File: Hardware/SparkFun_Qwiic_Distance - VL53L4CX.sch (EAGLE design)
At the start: 25 parts, among them J2 QWIIC_RIGHT_ANGLE, J4 QWIIC_RIGHT_ANGLE, U1 VL53L4X

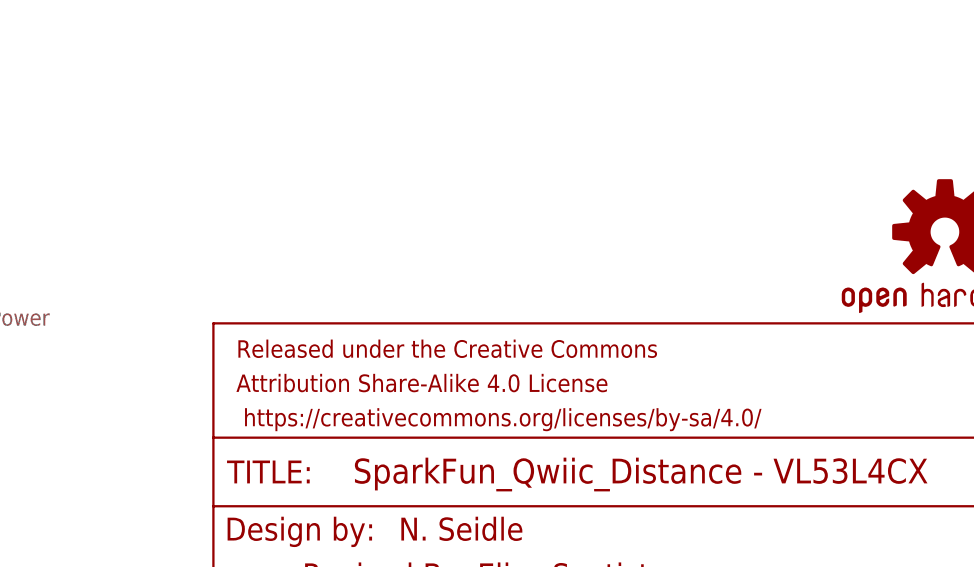
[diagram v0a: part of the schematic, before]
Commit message: Adds silk to the product
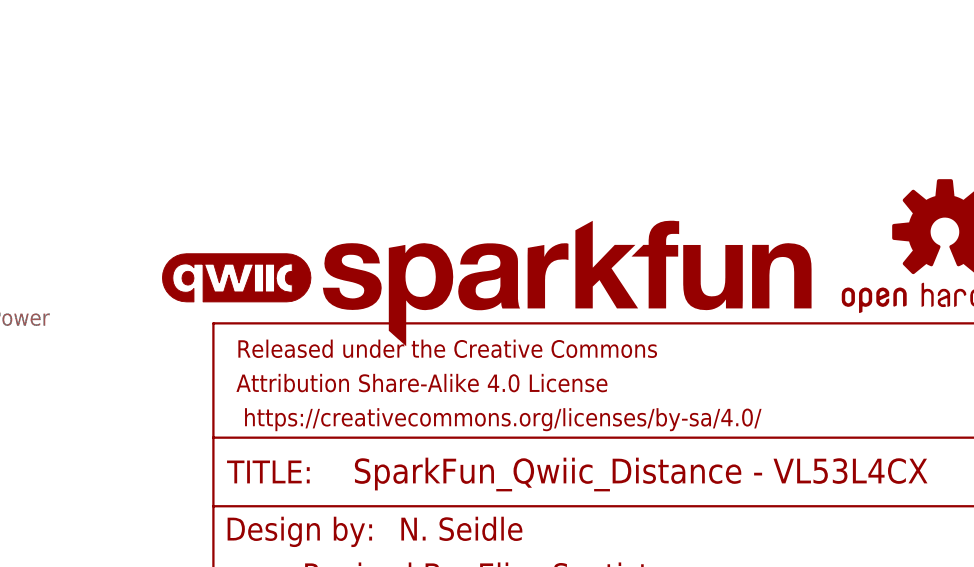
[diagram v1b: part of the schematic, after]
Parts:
- added LOGO2: SFE_LOGO_NAME.1_INCH, SparkFun-Aesthetics:SFE_LOGO_NAME.1_INCH
- added LOGO3: QWIIC_LOGO_4MM, SparkFun-Aesthetics:QWIIC_LOGO_4MM
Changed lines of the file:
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@@
 <part name="JP8" library="SparkFun" deviceset="STAND-OFF" device=""/>
 <part name="JP10" library="SparkFun-Jumpers" deviceset="JUMPER-SMT_2_NC_TRACE" device="_SILK" package3d_urn="urn:adsk.eagle:package:39281/1" value="INT"/>
+<part name="LOGO2" library="SparkFun-Aesthetics" deviceset="SFE_LOGO_NAME" device=".1_INCH"/>
+<part name="LOGO3" library="SparkFun-Aesthetics" deviceset="QWIIC_LOGO" device="_4MM"/>
 </parts>
 <sheets>
@@
 <attribute name="VALUE" x="122.682" y="29.464" size="1.778" layer="96" font="vector" rot="R180"/>
 </instance>
+<instance part="LOGO2" gate="G$1" x="157.48" y="33.02" smashed="yes"/>
+<instance part="LOGO3" gate="G$1" x="149.86" y="40.64" smashed="yes"/>
 </instances>
 <busses>

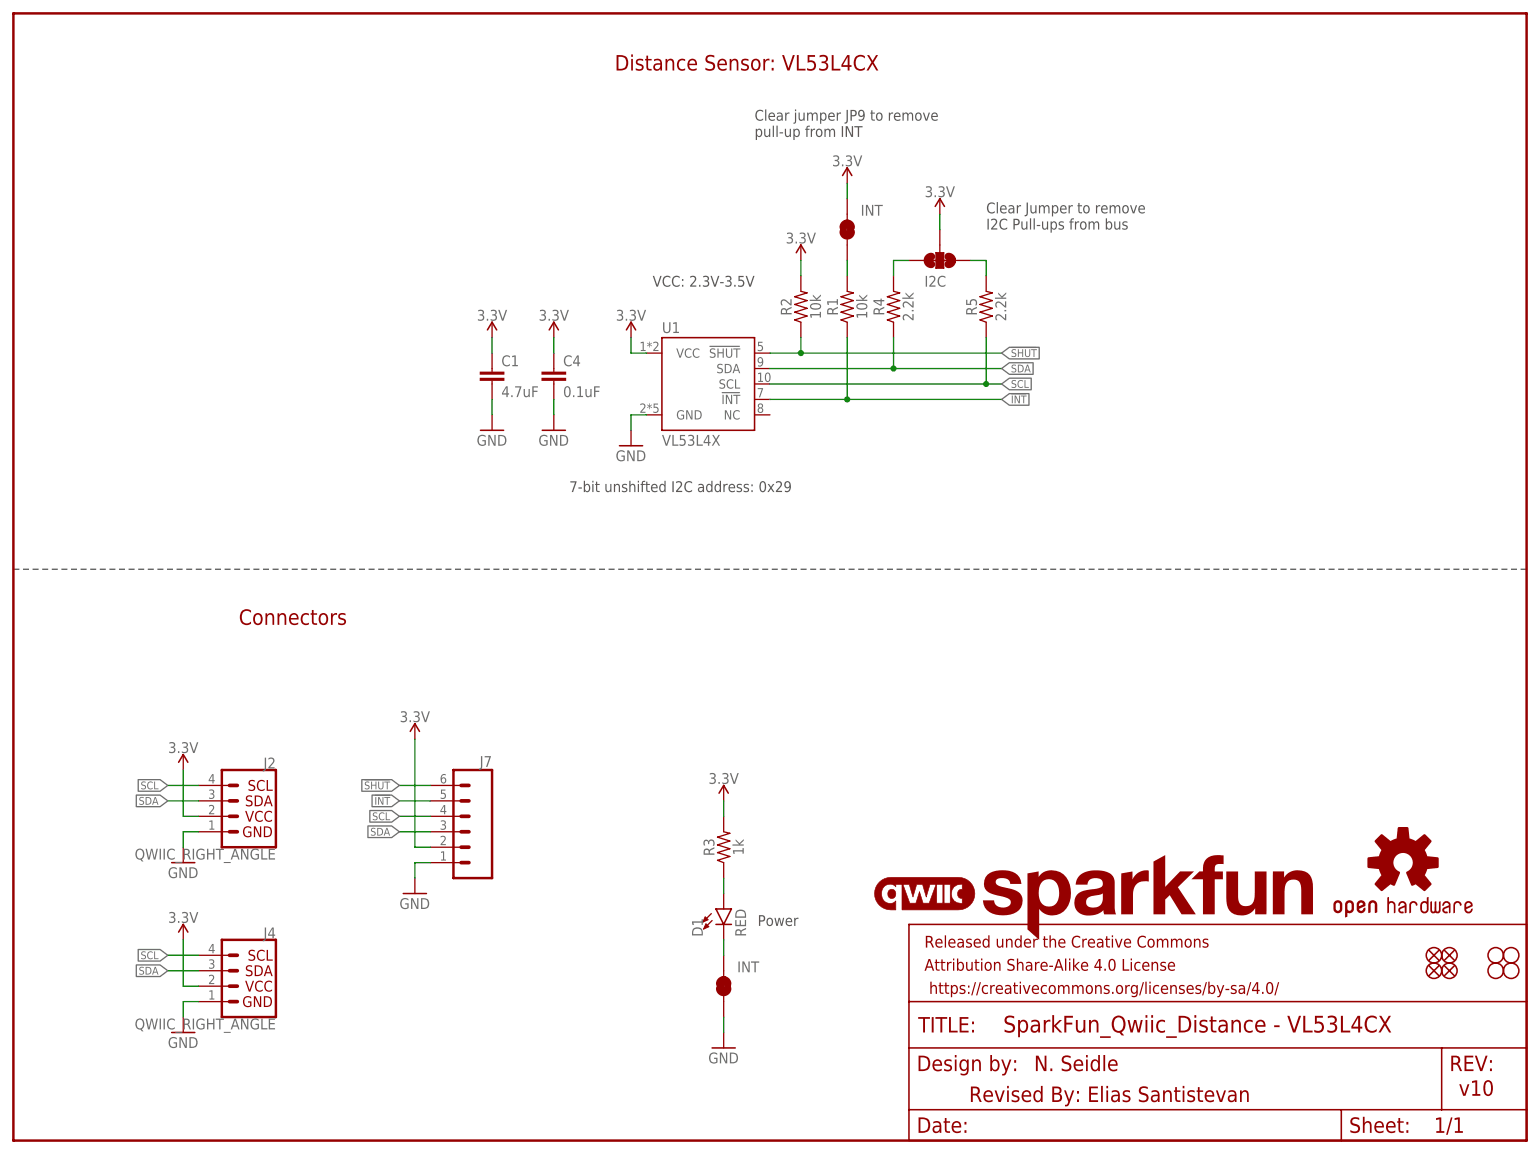
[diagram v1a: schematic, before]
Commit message: Replaces INT silk with OUTPUT style flag, adds revised by to attribution in board
* 3.3V traces bumped to 16mils
* Moves some silk to keep them from touching
* Adds PWR silk
* Adjusts some overlapping part labels
* Corrects distance sensor name in library
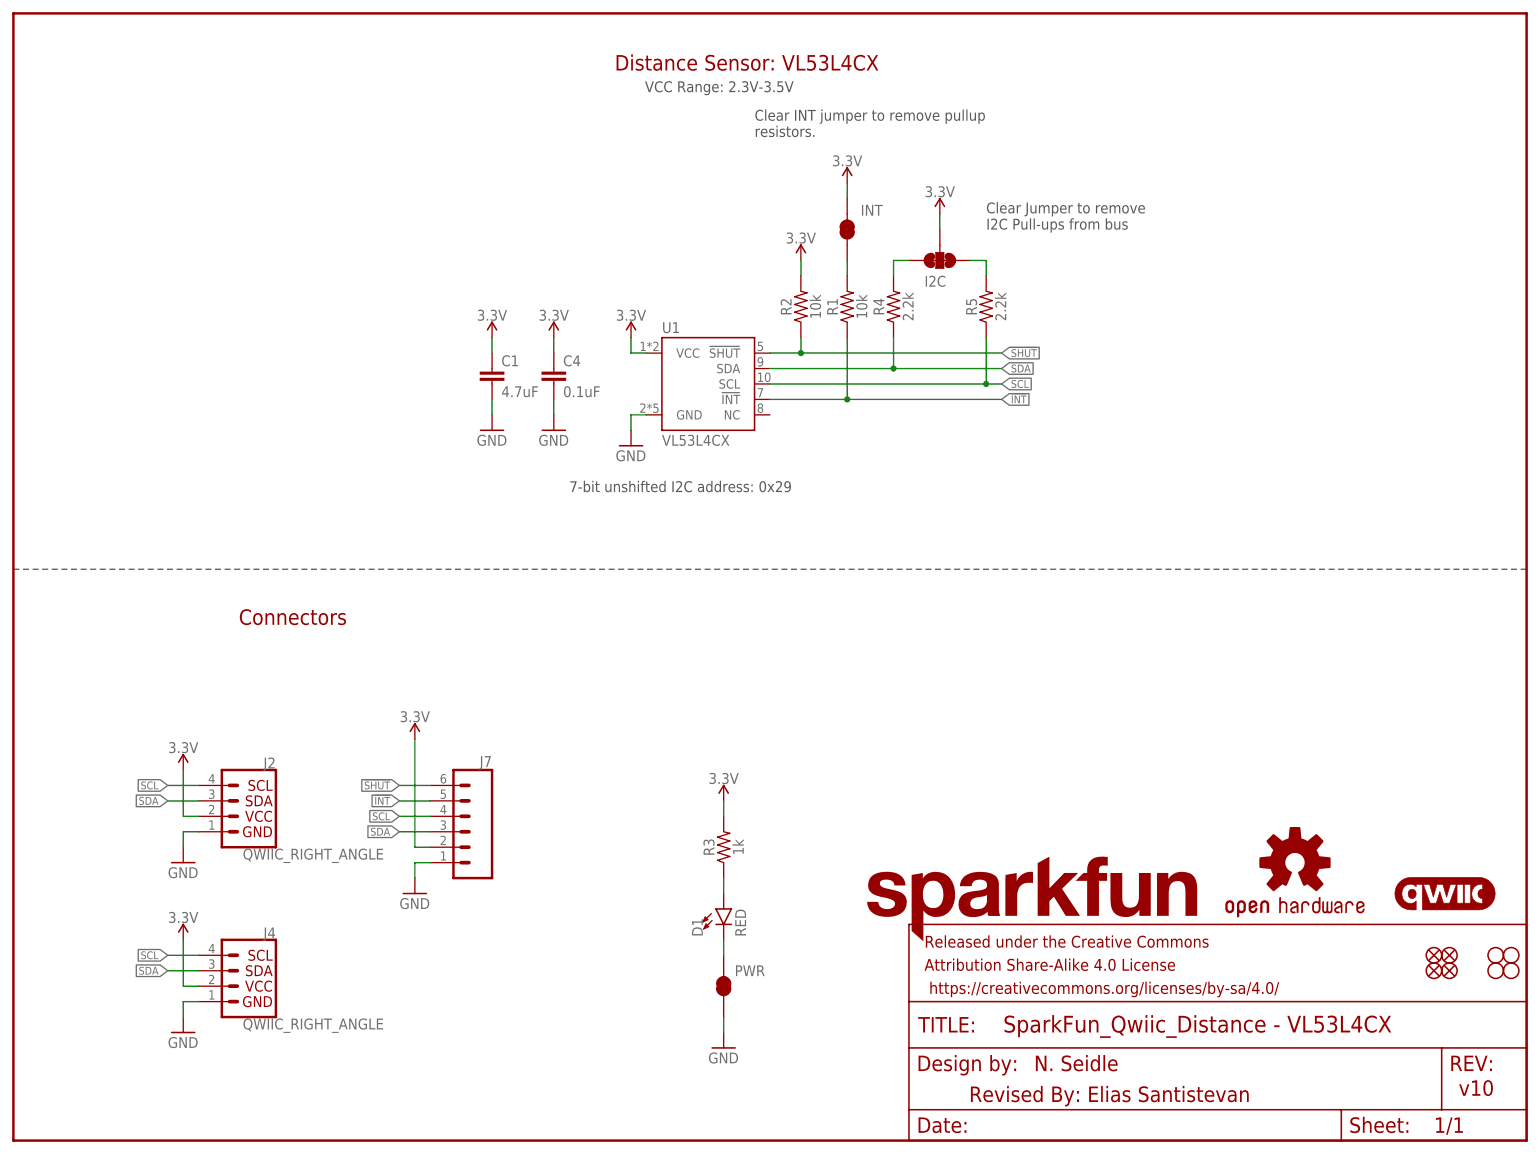
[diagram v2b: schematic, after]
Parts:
- U1: value VL53L4X -> VL53L4CX; device DISTANCE:VL53L4X -> DISTANCE:VL53L4CX
- renumbered JP10 to PWR
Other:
- note added: "Clear INT jumper to remove pullup resistors."
- note added: "VCC Range: 2.3V-3.5V"
- note removed: "Clear jumper JP9 to remove pull-up from INT"
- note removed: "Power"
- note removed: "VCC: 2.3V-3.5V"
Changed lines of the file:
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@@
 <part name="GND3" library="SparkFun-PowerSymbols" deviceset="GND" device=""/>
 <part name="FRAME1" library="SparkFun-Aesthetics" deviceset="FRAME-LETTER" device=""/>
-<part name="U1" library="DISTANCE" deviceset="VL53L4X" device=""/>
+<part name="U1" library="DISTANCE" deviceset="VL53L4CX" device=""/>
 <part name="J7" library="SparkFun-Connectors" deviceset="CONN_06" device="NO_SILK_NO_POP"/>
 <part name="SUPPLY11" library="SparkFun-PowerSymbols" deviceset="3.3V" device=""/>
@@
 <part name="JP7" library="SparkFun" deviceset="STAND-OFF" device=""/>
 <part name="JP8" library="SparkFun" deviceset="STAND-OFF" device=""/>
-<part name="JP10" library="SparkFun-Jumpers" deviceset="JUMPER-SMT_2_NC_TRACE" device="_SILK" package3d_urn="urn:adsk.eagle:package:39281/1" value="INT"/>
+<part name="PWR" library="SparkFun-Jumpers" deviceset="JUMPER-SMT_2_NC_TRACE" device="_SILK" package3d_urn="urn:adsk.eagle:package:39281/1" value="INT"/>
 <part name="LOGO2" library="SparkFun-Aesthetics" deviceset="SFE_LOGO_NAME" device=".1_INCH"/>
 <part name="LOGO3" library="SparkFun-Aesthetics" deviceset="QWIIC_LOGO" device="_4MM"/>
@@
 <text x="160.02" y="149.86" size="1.778" layer="97" font="vector">Clear Jumper to remove
 I2C Pull-ups from bus</text>
-<text x="121.92" y="165.1" size="1.778" layer="97" font="vector">Clear jumper JP9 to remove
-pull-up from INT</text>
-<text x="122.428" y="35.306" size="1.778" layer="97" font="vector">Power</text>
+<text x="121.92" y="165.1" size="1.778" layer="97" font="vector">Clear INT jumper to remove pullup
+resistors.</text>
 <wire x1="0" y1="93.98" x2="248.92" y2="93.98" width="0.1524" layer="97" style="longdash"/>
 <text x="45.974" y="86.106" size="2.54" layer="94" font="vector" align="center">Connectors</text>
 <text x="120.65" y="177.292" size="2.54" layer="94" font="vector" align="center">Distance Sensor: VL53L4CX</text>
-<text x="105.156" y="140.462" size="1.778" layer="97" font="vector">VCC: 2.3V-3.5V</text>
+<text x="103.886" y="172.466" size="1.778" layer="97" font="vector">VCC Range: 2.3V-3.5V</text>
 <text x="180.34" y="7.62" size="2.54" layer="94" font="vector" align="center">Revised By: Elias Santistevan</text>
 </plain>
@@
 </instance>
 <instance part="J2" gate="G$1" x="38.1" y="53.34" smashed="yes" rot="MR0">
-<attribute name="VALUE" x="43.18" y="48.006" size="1.778" layer="96" font="vector" rot="MR0" align="top-left"/>
+<attribute name="VALUE" x="60.96" y="48.006" size="1.778" layer="96" font="vector" rot="MR0" align="top-left"/>
 <attribute name="NAME" x="43.18" y="61.214" size="1.778" layer="95" font="vector" rot="MR0"/>
 </instance>
@@
 </instance>
 <instance part="J4" gate="G$1" x="38.1" y="25.4" smashed="yes" rot="MR0">
-<attribute name="VALUE" x="43.18" y="20.066" size="1.778" layer="96" font="vector" rot="MR0" align="top-left"/>
+<attribute name="VALUE" x="60.96" y="20.066" size="1.778" layer="96" font="vector" rot="MR0" align="top-left"/>
 <attribute name="NAME" x="43.18" y="33.274" size="1.778" layer="95" font="vector" rot="MR0"/>
 </instance>
@@
 <attribute name="VALUE" x="25.4" y="15.24" size="1.778" layer="96" font="vector"/>
 </instance>
-<instance part="LOGO1" gate="G$1" x="228.6" y="45.72" smashed="yes"/>
+<instance part="LOGO1" gate="G$1" x="210.82" y="45.72" smashed="yes"/>
 <instance part="R1" gate="G$1" x="137.16" y="137.16" smashed="yes" rot="R90">
 <attribute name="NAME" x="135.636" y="137.16" size="1.778" layer="95" font="vector" rot="R90" align="bottom-center"/>
@@
 <instance part="JP7" gate="G$1" x="243.84" y="30.48" smashed="yes"/>
 <instance part="JP8" gate="G$1" x="243.84" y="27.94" smashed="yes"/>
-<instance part="JP10" gate="G$1" x="116.84" y="25.4" smashed="yes" rot="R90">
-<attribute name="VALUE" x="122.682" y="29.464" size="1.778" layer="96" font="vector" rot="R180"/>
-</instance>
-<instance part="LOGO2" gate="G$1" x="157.48" y="33.02" smashed="yes"/>
-<instance part="LOGO3" gate="G$1" x="149.86" y="40.64" smashed="yes"/>
+<instance part="PWR" gate="G$1" x="116.84" y="25.4" smashed="yes" rot="R90">
+<attribute name="NAME" x="121.158" y="27.94" size="1.778" layer="95" font="vector" rot="R180" align="center"/>
+</instance>
+<instance part="LOGO2" gate="G$1" x="138.43" y="32.766" smashed="yes"/>
+<instance part="LOGO3" gate="G$1" x="235.458" y="40.64" smashed="yes"/>
 </instances>
 <busses>
@@
 </segment>
 <segment>
-<pinref part="JP10" gate="G$1" pin="1"/>
+<pinref part="PWR" gate="G$1" pin="1"/>
 <pinref part="GND3" gate="1" pin="GND"/>
 <wire x1="116.84" y1="20.32" x2="116.84" y2="17.78" width="0.1524" layer="91"/>
@@
 <net name="N$5" class="0">
 <segment>
-<pinref part="JP10" gate="G$1" pin="2"/>
+<pinref part="PWR" gate="G$1" pin="2"/>
 <pinref part="D1" gate="G$1" pin="C"/>
 <wire x1="116.84" y1="30.48" x2="116.84" y2="33.02" width="0.1524" layer="91"/>
